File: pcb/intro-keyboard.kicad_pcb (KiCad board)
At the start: 2 copper layers, 112 x 24 mm, 16 parts, among them SW1 RST, SW2 RotaryEncoder_Switch, SW3 RotaryEncoder_Switch, SW4 RotaryEncoder_Switch, SW5 RotaryEncoder_Switch, U1 Sea-Picro-RST

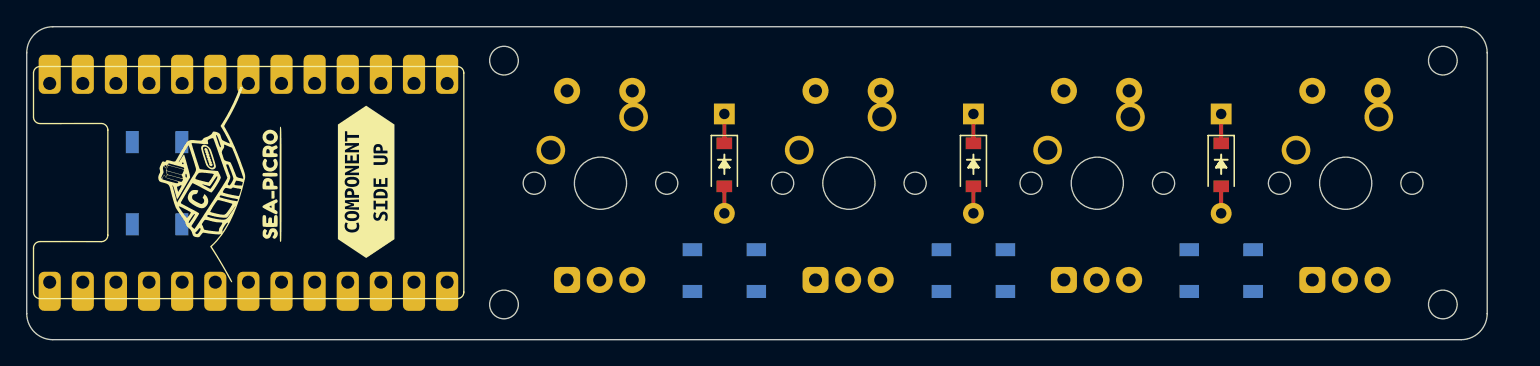
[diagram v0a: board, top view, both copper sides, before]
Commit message: add diodes to matrix
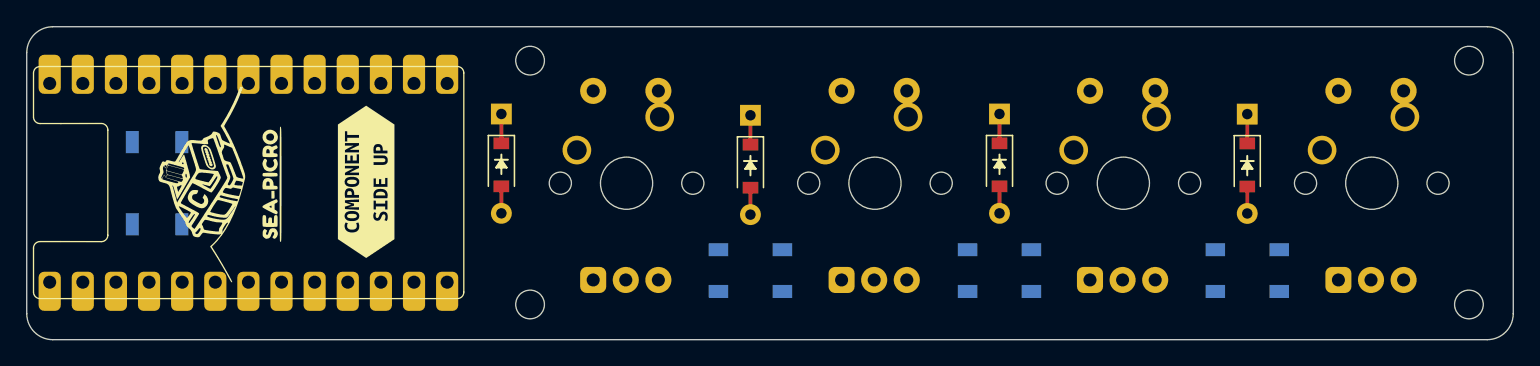
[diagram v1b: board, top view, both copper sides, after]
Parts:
- added D7: 1N4148, intro-footprints:dual_diode, F.Cu at (176.6, 74.7)
- moved D1 36.2 mm to (119.4, 74.7)
- moved D2 36.1 mm to (138.5, 74.8)
- moved D3 21.1 mm to (157.6, 74.7)
- moved D4 2.00 mm to (138.5, 86.7)
- moved D5 2.00 mm to (157.6, 86.7)
- moved D6 2.00 mm to (176.6, 86.7)
- moved H1 2.00 mm to (121.6, 70.6)
- moved H2 2.00 mm to (193.6, 89.3)
- moved H3 2.00 mm to (121.6, 89.3)
- moved H4 2.00 mm to (193.6, 70.6)
- moved SW2 2.00 mm to (128.9, 80.0)
- moved SW3 2.00 mm to (148.0, 80.0)
- moved SW4 2.00 mm to (167.0, 80.0)
- moved SW5 2.00 mm to (186.1, 80.0)
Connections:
- D1 pad 1: unconnected-(D1-Pad1) -> /SW_0
- D1 pad 2: unconnected-(D1-Pad2) -> /SW_0_DIODE
- D2 pad 1: unconnected-(D2-Pad1) -> /SW_1
- D2 pad 2: unconnected-(D2-Pad2) -> /SW_1_DIODE
- D3 pad 1: unconnected-(D3-Pad1) -> /SW_2
- D3 pad 2: unconnected-(D3-Pad2) -> /SW_2_DIODE
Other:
- board size 112 x 24 mm -> 114 x 24 mm

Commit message: finish schematic and lay out
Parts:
- added kibuzzard-62DD1F9A: G***, kibuzzard-62DD1F9A, B.Cu at (97.4, 80.0)
- moved D1 0.20 mm to (119.4, 74.9)
- moved D3 0.20 mm to (157.6, 74.9)
- moved D7 0.20 mm to (176.6, 74.9)
- moved D2 0.20 mm to (138.5, 75.0)
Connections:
- U1 pad 11: unconnected-(U1-Pad11) -> /LED
- U1 pad 12: unconnected-(U1-Pad12) -> /ENC_B
- U1 pad 13: unconnected-(U1-Pad13) -> /ENC_A
- U1 pad 19: unconnected-(U1-Pad19) -> /SW_0
- U1 pad 20: unconnected-(U1-Pad20) -> /SW_1
- U1 pad 21: unconnected-(U1-Pad21) -> /SW_2
- U1 pad 22: unconnected-(U1-Pad22) -> /SW_3
- U1 pad 23: unconnected-(U1-Pad23) -> /SW_3_DIODE
- U1 pad 24: unconnected-(U1-Pad24) -> /SW_2_DIODE
- U1 pad 25: unconnected-(U1-Pad25) -> /SW_1_DIODE
- U1 pad 26: unconnected-(U1-Pad26) -> /SW_0_DIODE
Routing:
- net +3V3: track 0.00 -> 90.9 mm
- net /SW_3: track 0.00 -> 90.5 mm
- net /ENC_B: track 0.00 -> 82.7 mm
- net /SW_3_DIODE: track 0.00 -> 79.0 mm
- net /ENC_A: track 0.00 -> 73.8 mm
- net /SW_2: track 0.00 -> 67.2 mm
- net /SW_2_DIODE: track 0.00 -> 61.6 mm
- net /SW_1_DIODE: track 0.00 -> 43.7 mm
- net /SW_1: track 0.00 -> 43.4 mm
- net /LED: track 0.00 -> 26.9 mm
- net /SW_0_DIODE: track 0.00 -> 26.1 mm
- net /SW_0: track 0.00 -> 19.9 mm
- net Net-(D4-Pad2): track 0.00 -> 15.5 mm
- net Net-(D5-Pad2): track 0.00 -> 15.4 mm
- net Net-(SW1-Pad1): track 0.00 -> 11.3 mm
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- added copper zone on B.Cu, net GND
- added copper zone on F.Cu, net GND

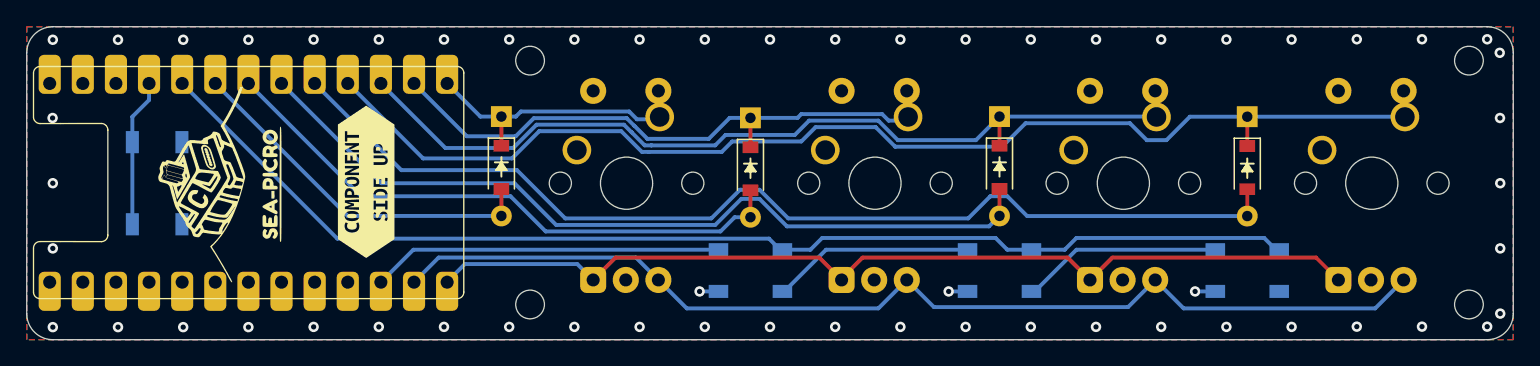
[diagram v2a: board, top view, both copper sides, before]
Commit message: add silk, teardrops
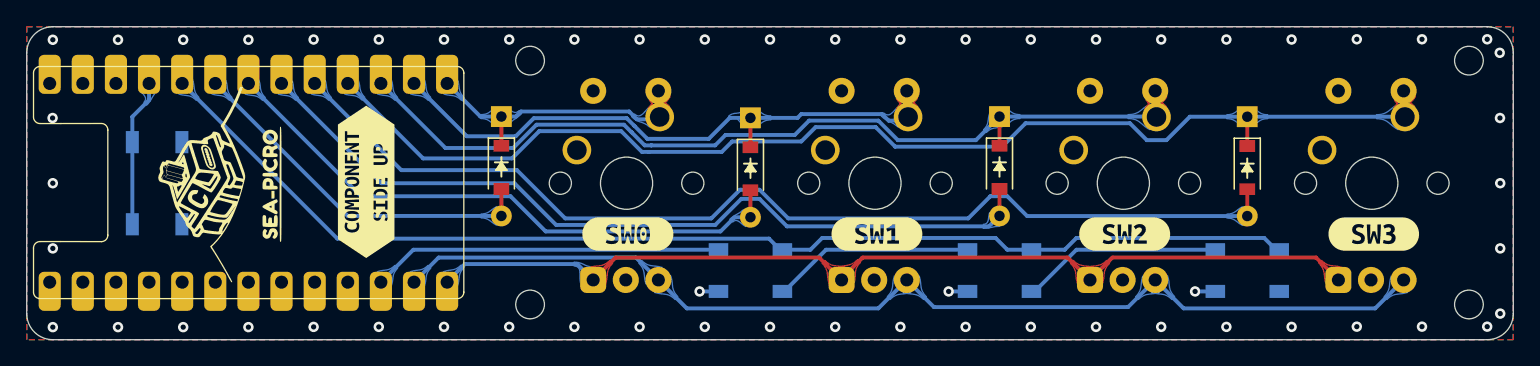
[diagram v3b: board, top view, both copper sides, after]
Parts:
- added kibuzzard-62DE70D8: G***, kibuzzard-62DE70D8, F.Cu at (129.1, 83.9)
- added kibuzzard-62DE70E0: G***, kibuzzard-62DE70E0, F.Cu at (148.2, 83.9)
- added kibuzzard-62DE70F4: G***, kibuzzard-62DE70F4, F.Cu at (167.2, 83.9)
- added kibuzzard-62DE7100: G***, kibuzzard-62DE7100, F.Cu at (186.3, 83.9)
